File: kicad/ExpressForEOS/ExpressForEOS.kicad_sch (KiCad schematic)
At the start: 10 parts, among them J1 Conn_02x17_Counter_Clockwise, U11 74LS156, U12 74LS156, U13 74LS373, U14 ICM7218BIPI, U15 MAX150BCPP, U6 74LS138, U7 74LS374, U8 74LS374, U9 74LS245

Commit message: more schematic updates, another datasheet
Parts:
- added U10: 74LS08, symbol 74xx:74LS08
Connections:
- net CTL0 is gone; now on an unnamed net: U6.15 (O0)
- net CTL1 is gone; now on an unnamed net: U6.14 (O1)
- net CTL3 is gone; now on an unnamed net: U6.12 (O3)
- net CTL4 is gone; now on an unnamed net: U6.11 (O4)
- net CTL5 is gone; now on an unnamed net: U6.10 (O5)
- net CTL6 is gone; now on an unnamed net: U6.9 (O6)
- net at U11.14 (Eb1): now also U11.2 (Ea2), U10.2
- net at U12.14 (Eb1): now also U12.2 (Ea2), U10.1
- net CTL10 renamed KEY_SCAN2
- net CTL11 renamed KEY_SCAN3
- net CTL12 renamed KEY_SCAN4
- net CTL13 renamed KEY_SCAN5
- net CTL14 renamed KEY_SCAN6
- net CTL15 renamed KEY_SCAN7
- net CTL16 renamed EXT0
- net CTL17 renamed EXT1
- net CTL18 renamed EXT2
- net CTL19 renamed EXT3
- net CTL2: no longer names the net of U6.13 (O2)
- net CTL20 renamed KEY_SCAN8
- net CTL21 renamed JMP
- net CTL22: no longer names the net of U12.11 (Q2b)
- net CTL23: no longer names the net of U12.12 (Q3b)
- net CTL7: no longer names the net of U6.7 (O7)
- net CTL8 renamed KEY_SCAN0
- net CTL9 renamed KEY_SCAN1
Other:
- moved on the sheet: J1, U11, U12, U13, U14, U15, U6, U7, U8, U9

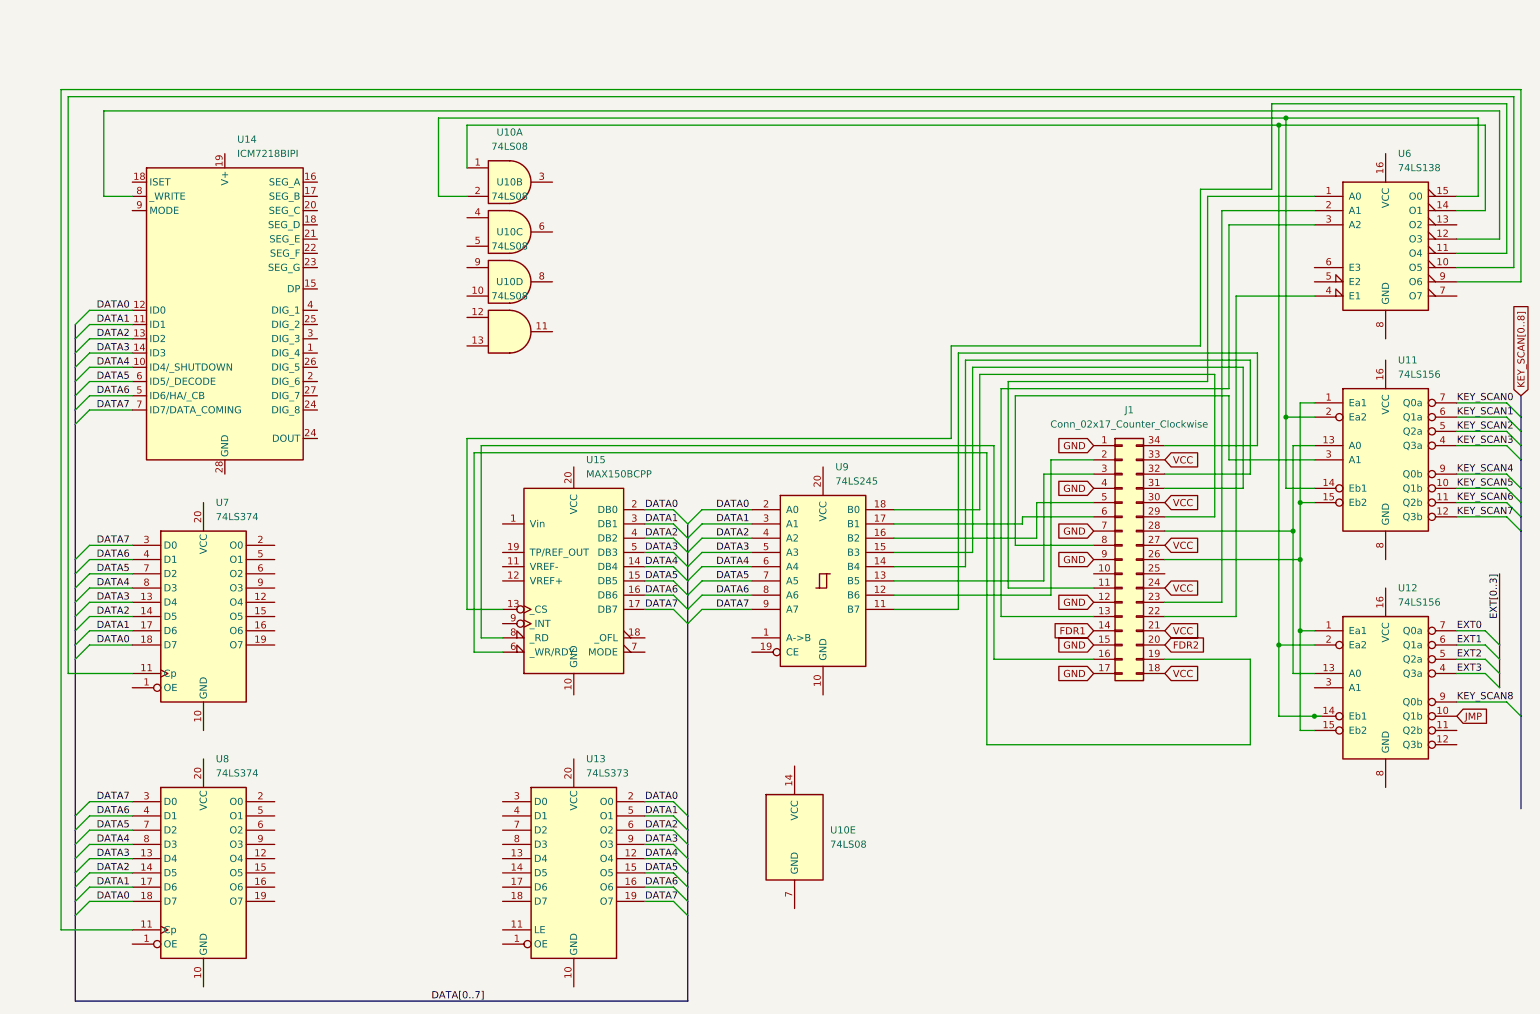
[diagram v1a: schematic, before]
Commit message: More schematic work, more datasheets
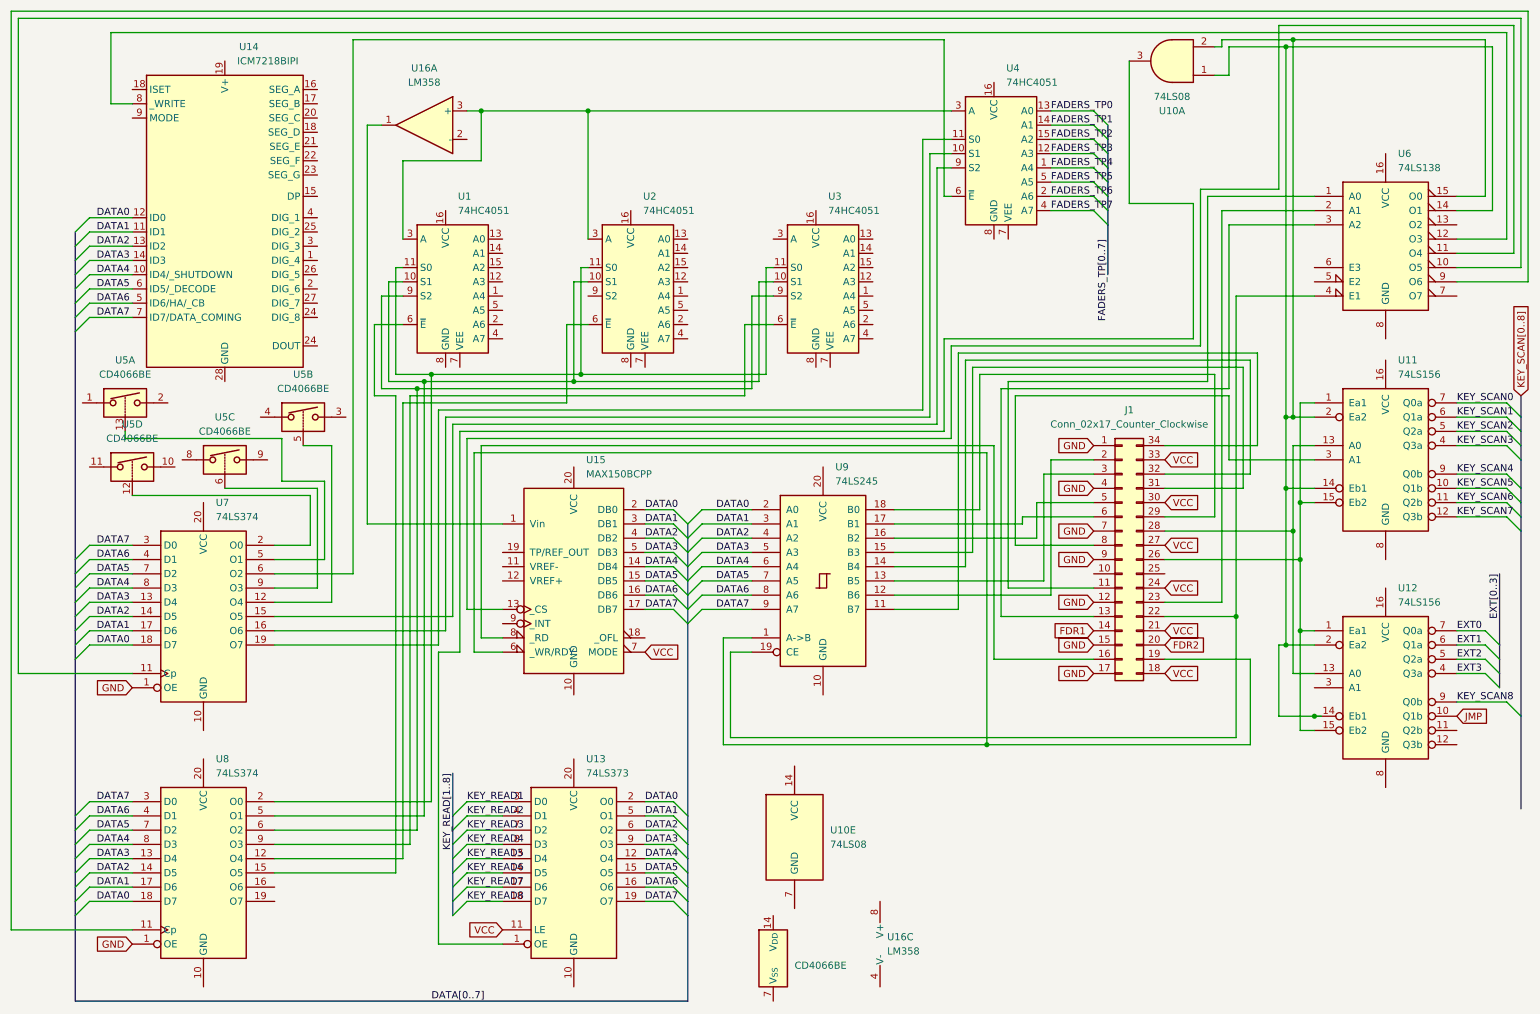
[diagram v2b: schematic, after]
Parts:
- removed unit 3 of U10
- removed unit 4 of U10
- removed unit 2 of U10
- added U1, U2, U3, U4: 74HC4051, symbol 74xx:74HC4051
- added U16: LM358, symbol Amplifier_Operational:LM358
- added U5: CD4066BE, Package_DIP:DIP-14_W7.62mm, symbol Analog_Switch:CD4066BE
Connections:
- net GND: now also U7.1 (OE), U8.1 (OE)
- net VCC: now also U13.11 (LE), U15.7 (MODE)
- net at U10.2, U11.14 (Eb1), U11.2 (Ea2)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: now also U10.1, U12.14 (Eb1), U12.2 (Ea2), U6.14 (O1)
- net at U8.12 (O4): now also U2.6 (~{E})
- net at U8.15 (O5): now also U1.6 (~{E})
- net at U8.2 (O0): now also U1.11 (S0), U2.11 (S0), U3.11 (S0)
- net at U8.5 (O1): now also U1.10 (S1), U2.10 (S1), U3.10 (S1)
- net at U8.6 (O2): now also U1.9 (S2), U3.9 (S2)
- net at U8.9 (O3): now also U3.6 (~{E})
- net at U13.1 (OE): now also U10.3
- net KEY_READ5: now reaches U13.13 (D4)
- net KEY_READ6: now reaches U13.14 (D5)
- net KEY_READ7: now reaches U13.17 (D6)
- net KEY_READ8: now reaches U13.18 (D7)
- net KEY_READ1: now reaches U13.3 (D0)
- net KEY_READ2: now reaches U13.4 (D1)
- net KEY_READ3: now reaches U13.7 (D2)
- net KEY_READ4: now reaches U13.8 (D3)
- net at U7.12 (O4): now also U5.5
- net at U7.15 (O5): now also U4.9 (S2)
- net at U7.16 (O6): now also U4.10 (S1)
- net at U7.19 (O7): now also U4.11 (S0)
- net at U7.2 (O0): now also U5.12
- net at U7.5 (O1): now also U5.13
- net at U7.6 (O2): now also U4.6 (~{E})
- net at U7.9 (O3): now also U5.6
- net at J1.22 (Pin_22), U6.4 (E1): now also U9.19 (CE)
- net at U15.1 (Vin): now also U16.1
- net at J1.19 (Pin_19), U15.6 (_WR/RDY): now also U9.1 (A->B)
- new net: U1.3 (A), U16.3 (+), U2.3 (A), U4.3 (A)
- new net FADERS_TP0: U4.13 (A0)
- new net FADERS_TP1: U4.14 (A1)
- new net FADERS_TP2: U4.15 (A2)
- new net FADERS_TP3: U4.12 (A3)
- new net FADERS_TP4: U4.1 (A4)
- new net FADERS_TP5: U4.5 (A5)
- new net FADERS_TP6: U4.2 (A6)
- new net FADERS_TP7: U4.4 (A7)
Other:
- moved on the sheet: U10A, U14

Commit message: Fixed a wire
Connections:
- net at U1.3 (A), U16.3 (+), U2.3 (A)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: now also U3.3 (A)
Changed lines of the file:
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@@
   (junction (at 115.57 77.47) (diameter 0) (color 0 0 0 0)
   )
+  (junction (at 148.59 30.48) (diameter 0) (color 0 0 0 0)
+  )
   (junction (at 243.84 100.33) (diameter 0) (color 0 0 0 0)
   )
@@
     (stroke (width 0) (type default))
   )
+  (wire (pts (xy 148.59 53.34) (xy 148.59 30.48))
+    (stroke (width 0) (type default))
+  )
   (wire (pts (xy 27.94 125.73) (xy 35.56 125.73))
     (stroke (width 0) (type default))
@@
     (stroke (width 0) (type default))
   )
-  (wire (pts (xy 116.84 30.48) (xy 181.61 30.48))
+  (wire (pts (xy 116.84 30.48) (xy 148.59 30.48))
     (stroke (width 0) (type default))
   )
@@
     (stroke (width 0) (type default))
   )
+  (wire (pts (xy 148.59 30.48) (xy 181.61 30.48))
+    (stroke (width 0) (type default))
+  )
   (wire (pts (xy 116.84 30.48) (xy 116.84 53.34))
     (stroke (width 0) (type default))
@@
     (stroke (width 0) (type default))
   )
+  (wire (pts (xy 149.86 53.34) (xy 148.59 53.34))
+    (stroke (width 0) (type default))
+  )

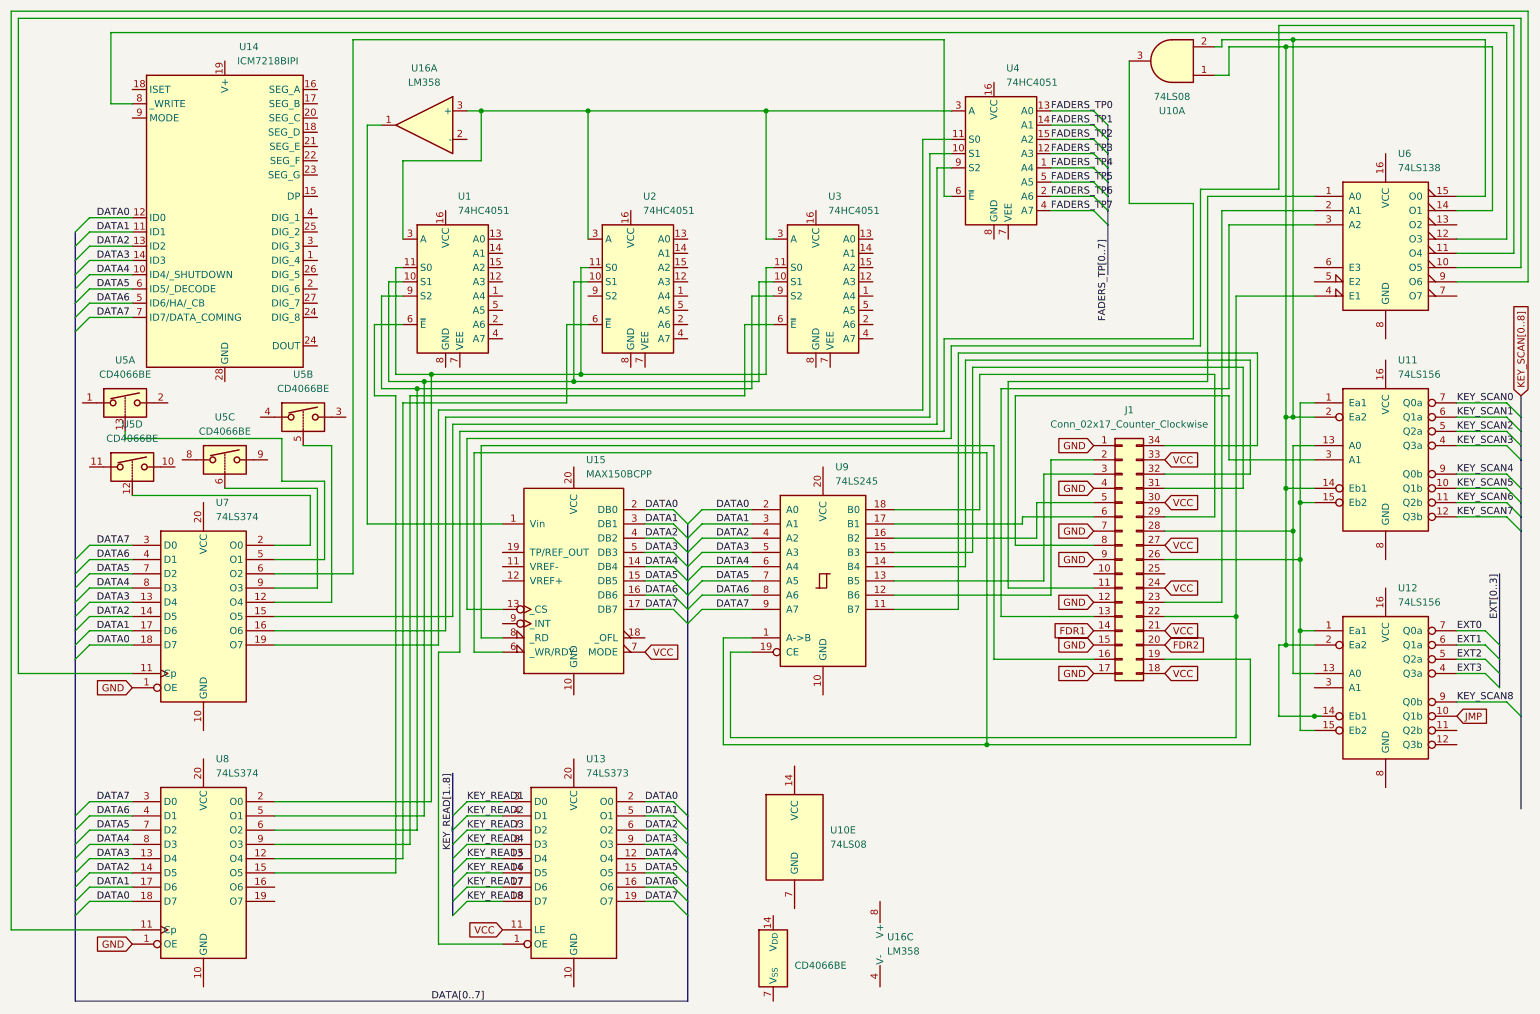
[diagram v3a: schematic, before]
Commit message: converted some nets to busses for clarity
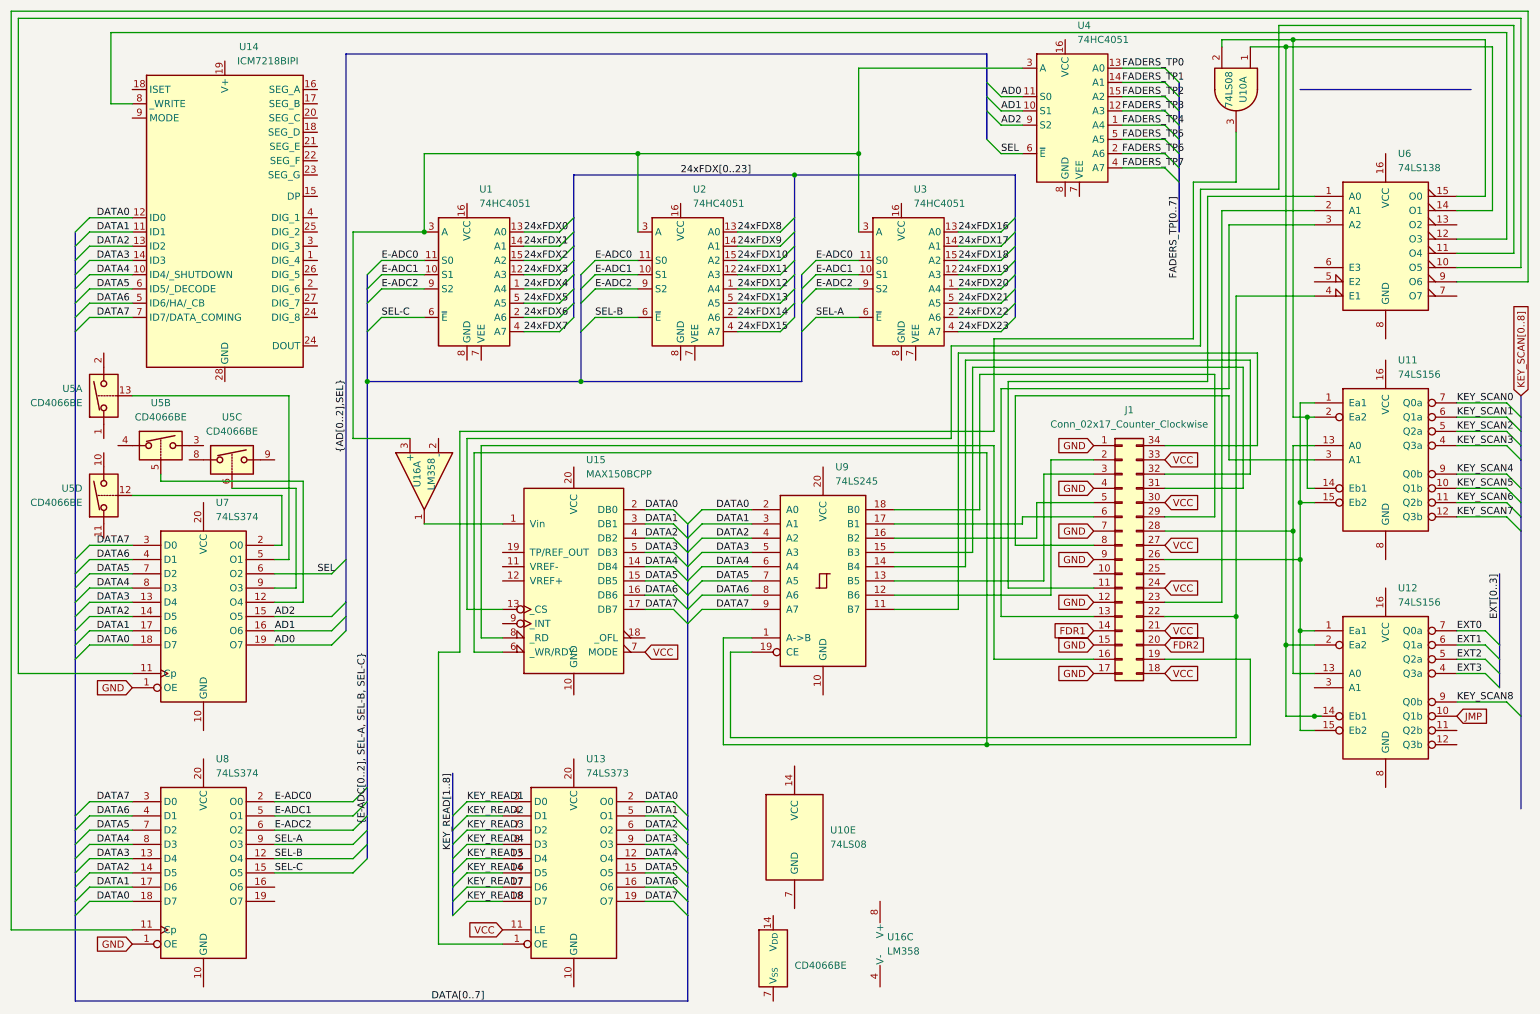
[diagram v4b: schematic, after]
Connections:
- net at U10.2, U11.14 (Eb1), U11.2 (Ea2)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: no longer U10.1, U12.14 (Eb1), U12.2 (Ea2), U6.14 (O1)
- net AD1: now reaches U4.10 (S1), U7.16 (O6)
- net AD0: now reaches U4.11 (S0), U7.19 (O7)
- net SEL: now reaches U4.6 (~{E}), U7.6 (O2)
- net AD2: now reaches U4.9 (S2), U7.15 (O5)
- net 24xFDX4: now reaches U1.1 (A4)
- net E-ADC1: now reaches U1.10 (S1), U2.10 (S1), U3.10 (S1), U8.5 (O1)
- net E-ADC0: now reaches U1.11 (S0), U2.11 (S0), U3.11 (S0), U8.2 (O0)
- net 24xFDX3: now reaches U1.12 (A3)
- net 24xFDX0: now reaches U1.13 (A0)
- net 24xFDX1: now reaches U1.14 (A1)
- net 24xFDX2: now reaches U1.15 (A2)
- net 24xFDX6: now reaches U1.2 (A6)
- net 24xFDX7: now reaches U1.4 (A7)
- net 24xFDX5: now reaches U1.5 (A5)
- net SEL-C: now reaches U1.6 (~{E}), U8.15 (O5)
- net E-ADC2: now reaches U1.9 (S2), U3.9 (S2), U8.6 (O2)
- net E-ADC2: now also U2.9 (S2)
- net SEL-B: now reaches U2.6 (~{E}), U8.12 (O4)
- net SEL-A: now reaches U3.6 (~{E}), U8.9 (O3)
- net 24xFDX20: now reaches U3.1 (A4)
- net 24xFDX19: now reaches U3.12 (A3)
- net 24xFDX16: now reaches U3.13 (A0)
- net 24xFDX17: now reaches U3.14 (A1)
- net 24xFDX18: now reaches U3.15 (A2)
- net 24xFDX22: now reaches U3.2 (A6)
- net 24xFDX23: now reaches U3.4 (A7)
- net 24xFDX21: now reaches U3.5 (A5)
- net 24xFDX12: now reaches U2.1 (A4)
- net 24xFDX11: now reaches U2.12 (A3)
- net 24xFDX8: now reaches U2.13 (A0)
- net 24xFDX9: now reaches U2.14 (A1)
- net 24xFDX10: now reaches U2.15 (A2)
- net 24xFDX14: now reaches U2.2 (A6)
- net 24xFDX15: now reaches U2.4 (A7)
- net 24xFDX13: now reaches U2.5 (A5)
- new net: U10.1, U12.14 (Eb1), U12.2 (Ea2), U6.14 (O1)
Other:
- moved on the sheet: U1, U10A, U16A, U2, U3, U4, U5A, U5B, U5C, U5D

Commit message: More tidy-up work
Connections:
- net at U11.13 (A0), U12.13 (A0): no longer J1.28 (Pin_28)
- net at U10.1, U12.14 (Eb1), U12.2 (Ea2)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: now also J1.28 (Pin_28)
- net B7: now reaches J1.34 (Pin_34), U9.11 (B7)
- net B6: now reaches J1.2 (Pin_2), U9.12 (B6)
- net B5: now reaches J1.3 (Pin_3), U9.13 (B5)
- net B4: now reaches J1.32 (Pin_32), U9.14 (B4)
- net B3: now reaches J1.31 (Pin_31), U9.15 (B3)
- net B2: now reaches J1.5 (Pin_5), U9.16 (B2)
- net B1: now reaches J1.6 (Pin_6), U9.17 (B1)
- net B0: now reaches J1.29 (Pin_29), U9.18 (B0)
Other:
- moved on the sheet: U10A, U16A

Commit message: Schem update
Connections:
- net SW1: now reaches U5.12, U7.2 (O0)
- net SW4: now reaches U5.5, U7.12 (O4)
- net SW2: now reaches U5.13, U7.5 (O1)
- net SW3: now reaches U5.6, U7.9 (O3)
- net KEY_READ1 renamed KEY_R1
- net KEY_READ2 renamed KEY_R2
- net KEY_READ3 renamed KEY_R3
- net KEY_READ4 renamed KEY_R4
- net KEY_READ5 renamed KEY_R5
- net KEY_READ6 renamed KEY_R6
- net KEY_READ7 renamed KEY_R7
- net KEY_READ8 renamed KEY_R8
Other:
- moved on the sheet: U16A, U5A, U5B, U5C, U5D
